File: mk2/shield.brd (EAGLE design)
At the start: 83.8 x 55.9 mm, 51 parts, among them P0 CON_DIL_20, P1 CON_DIL_20, P2 CON_DIL_20, P3 CON_DIL_20, P4 CON_DIL_20, P5 CON_DIL_20, Q1 20M

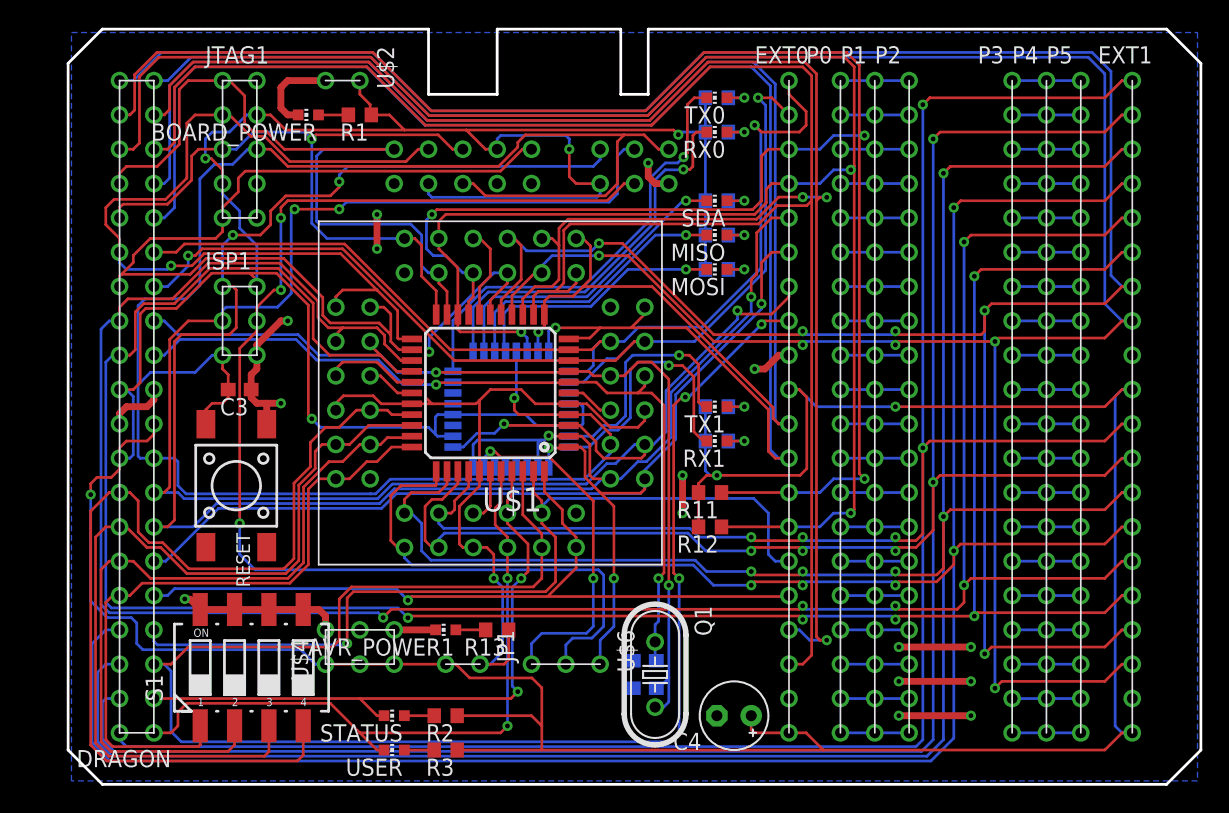
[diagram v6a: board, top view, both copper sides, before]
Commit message: [fix mk2 power connector]
	- move the power connector to the dragon board to match the actual
	  position  on the dragon
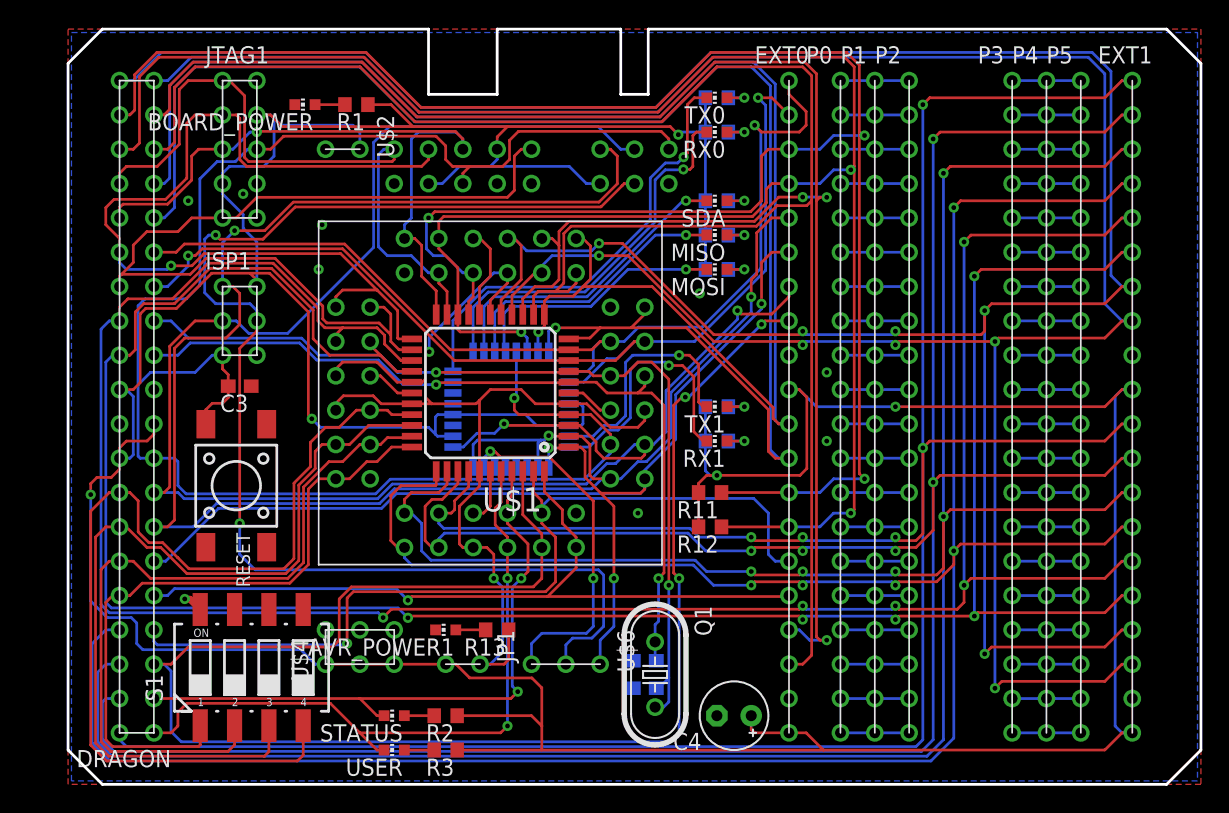
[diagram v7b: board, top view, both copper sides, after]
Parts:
- moved U$2 5.08 mm to (20.3, 53.3)
- moved BOARD_POWER 0.80 mm to (18.8, 56.6)
- moved R1 0.80 mm to (22.6, 56.6)
- moved C3 0.25 mm to (14.0, 35.8)
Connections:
- net GND: now also RESET.2
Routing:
- net GND: track 82.2 -> 19.5 mm, vias 15 -> 9
- net /RESET: track 143.6 -> 131.7 mm
- net TCK: track 55.7 -> 49.0 mm
- net MOSI: track 90.3 -> 96.8 mm, vias 3 -> 2
- net VCC: track 362.6 -> 357.5 mm, vias 7 -> 5
- net TDO: track 65.5 -> 68.1 mm
- net MISO: track 137.8 -> 140.0 mm, vias 4 -> 3
- net SCK: track 131.8 -> 132.6 mm, vias 4 -> 2
- net TMS: track 50.9 -> 50.2 mm
- added copper zone on layer 1, net GND

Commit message: [fix mk2 power out connector]
	- move the power out connector as well as the avr power and the
	  miso select headers to avoid overlap with the switches
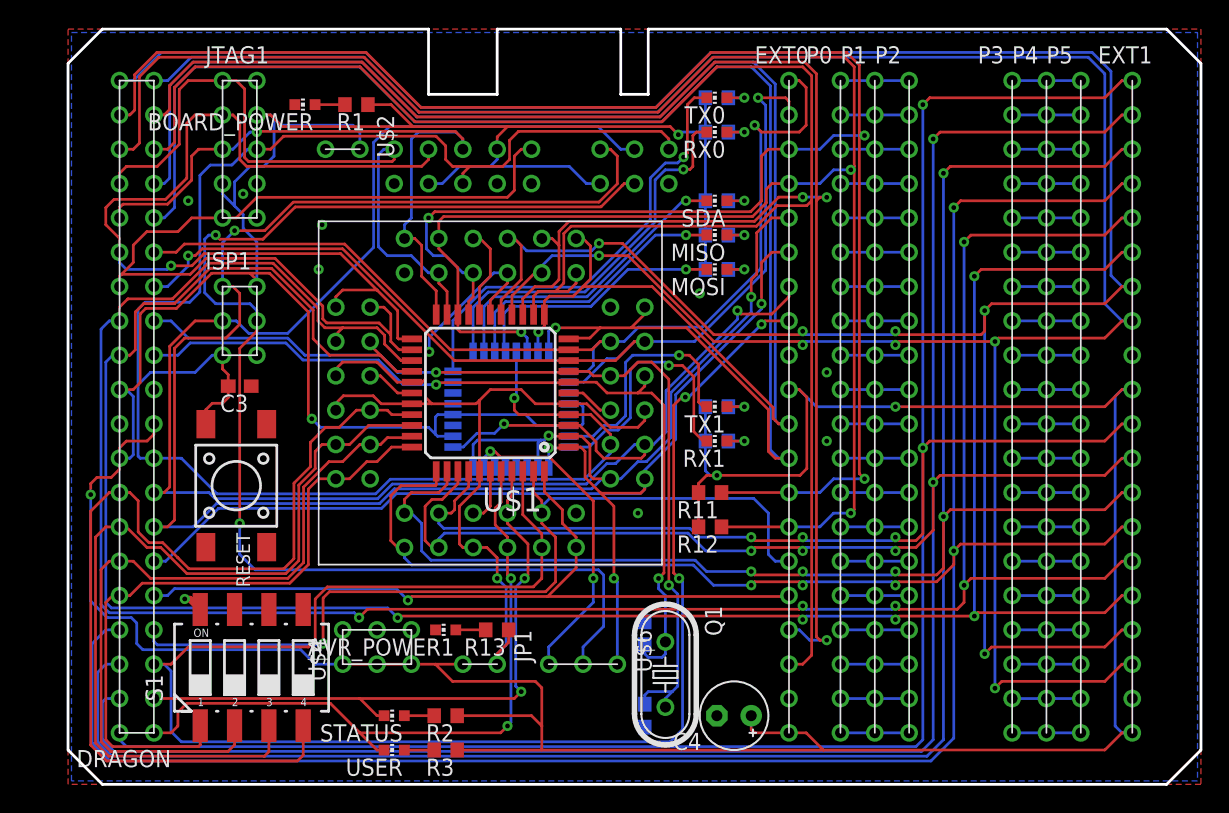
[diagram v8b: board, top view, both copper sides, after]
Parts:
- moved C1 2.03 mm to (43.9, 11.4), turned to 90 degrees
- moved C2 2.03 mm to (43.9, 17.5), turned to 270 degrees
- moved JP1 1.27 mm to (30.5, 15.2)
- moved U$4 1.27 mm to (24.1, 16.5)
- moved U$6 1.27 mm to (39.4, 15.2)
- moved Q1 0.76 mm to (45.5, 14.5)
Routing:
- net MOSI_MEGA88: track 26.4 -> 24.0 mm
- net VCC: track 357.5 -> 360.0 mm
- net VCC_MEGA1284: track 79.2 -> 76.9 mm
- net XTAL2: track 60.9 -> 62.8 mm
- net XTAL1: track 67.1 -> 68.5 mm
- net MOSI: track 96.8 -> 95.5 mm
- net /RESET: track 131.7 -> 131.0 mm
- net RX0: track 75.7 -> 76.3 mm
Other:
- board text added: "LED"
- board text added: "MAIN"
- board text removed: "MEGA1284"
- board text removed: "MEGA88"
